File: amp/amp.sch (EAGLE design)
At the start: 73 parts, among them IC1 OPA2134PA, Q1 BC547, Q10 IRF540, Q11 BC556, Q12 BC556, Q13 BC547, Q14 BC547, Q15 2N7000, Q16 BC337, Q17 BC337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

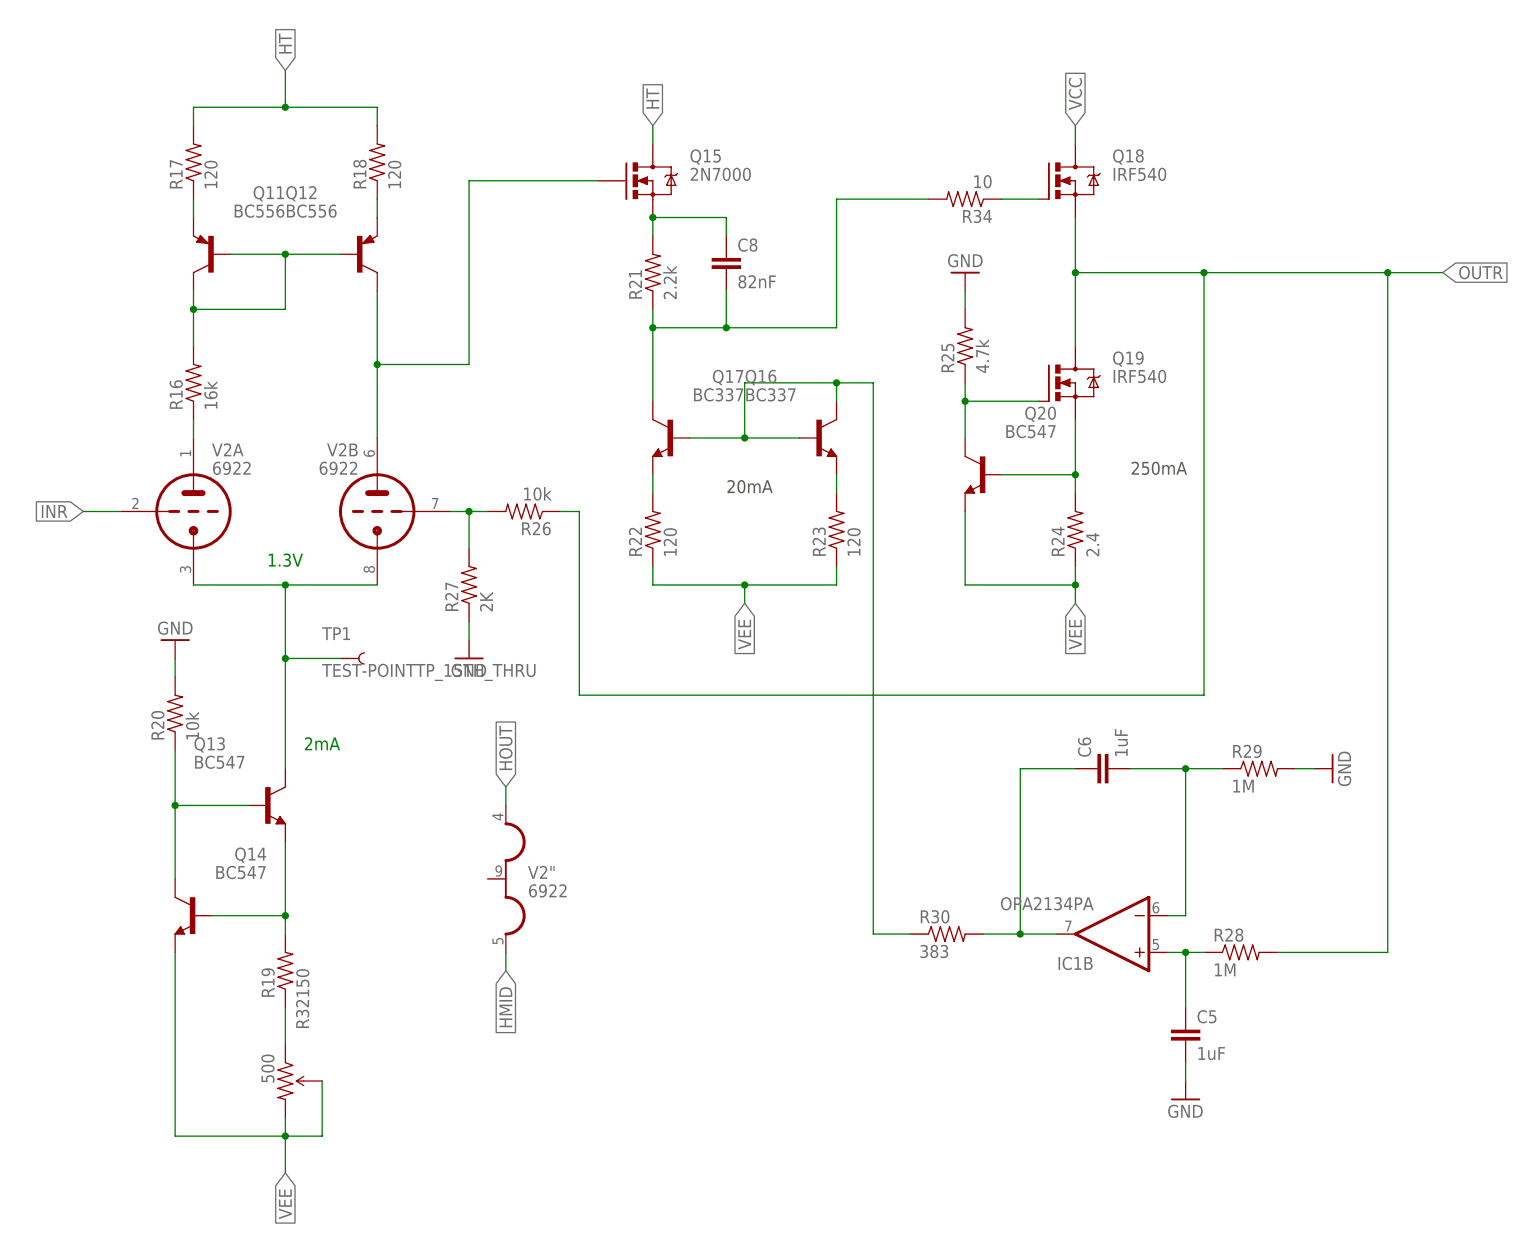
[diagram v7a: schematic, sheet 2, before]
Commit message: High frequency snubber
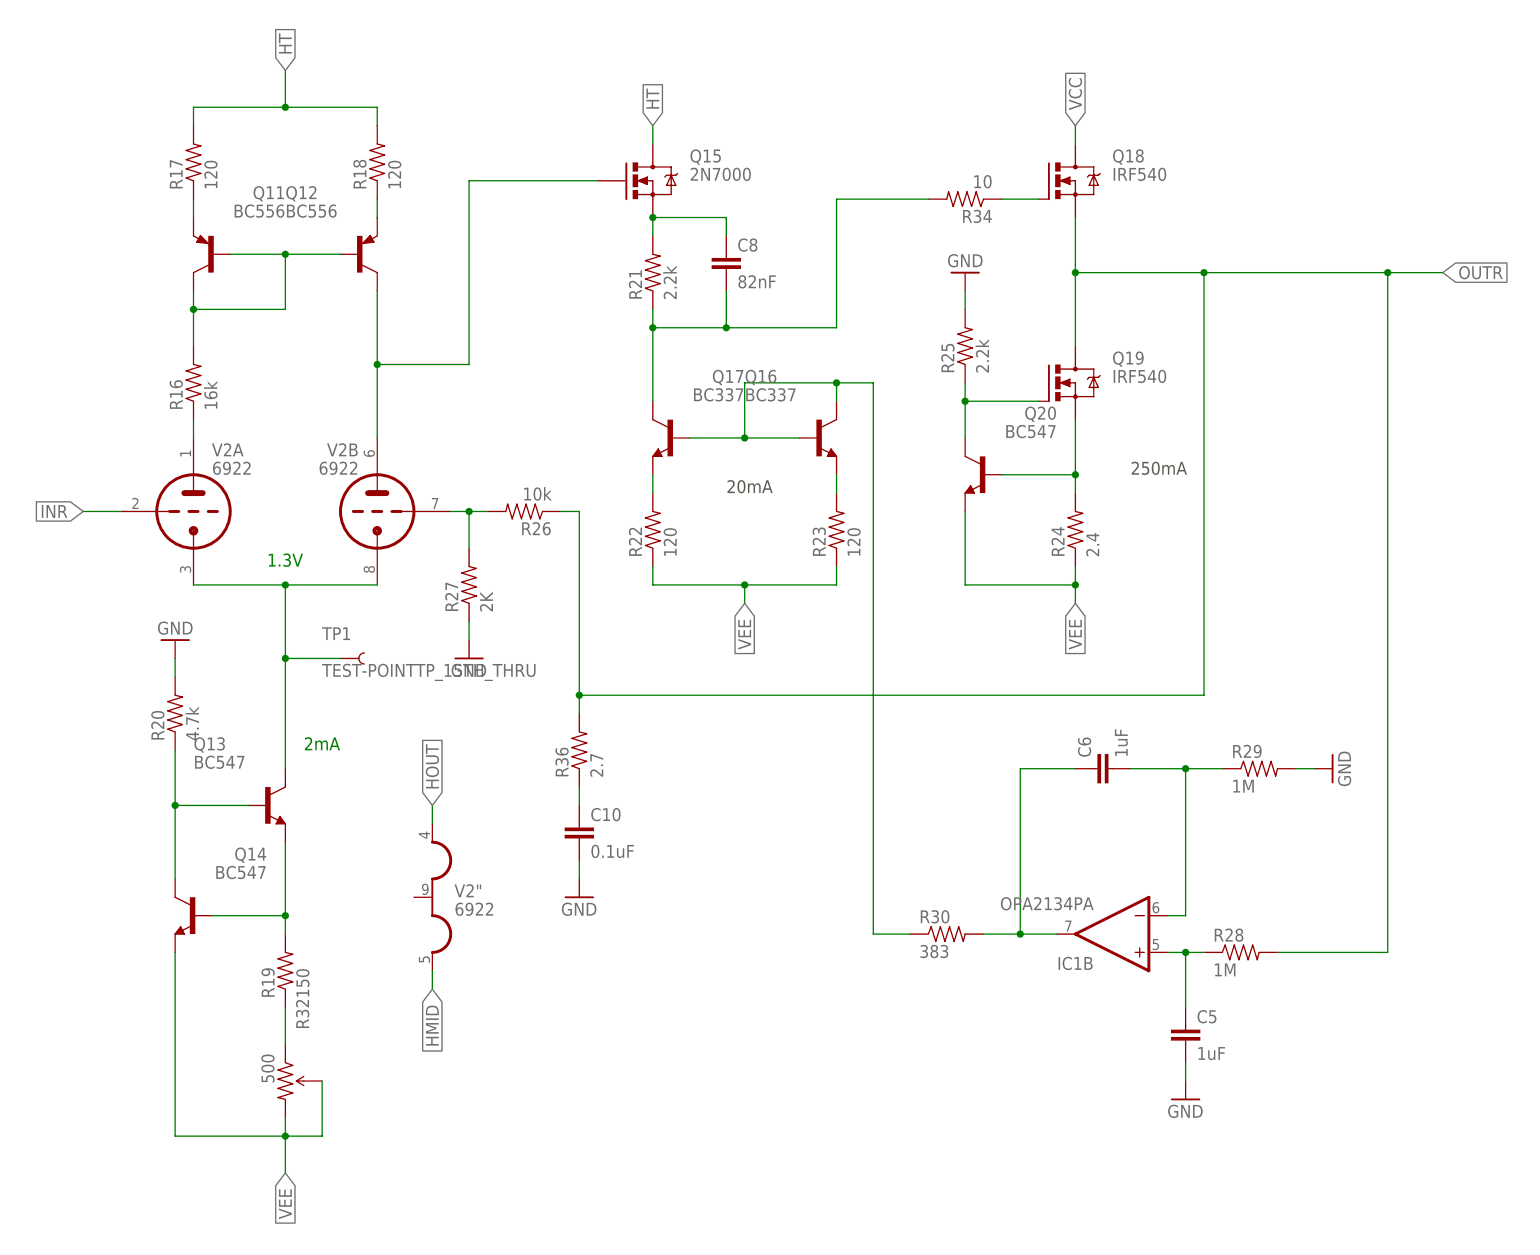
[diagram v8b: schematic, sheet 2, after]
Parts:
- added C10, C9: 0.1uF, SparkFun-Capacitors:0.1UF-25V(+80/-20%)(0603)
- added R35, R36: 2.7, SparkFun-Resistors:RESISTORPTH-1/4W
- R1, R20: value 10k -> 4.7k
- R12: value 10k -> 2.2k
- R25: value 4.7k -> 2.2k
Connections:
- new net N$43: C9.1, R35.1
- new net N$44: C10.1, R36.1
- net GND: now also C10.2, C9.2
- net OUTL: now also R35.2
- net OUTR: now also R36.2
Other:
- moved on the sheet: V2"
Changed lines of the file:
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@@
 <part name="Q1" library="transistor-npn" deviceset="BC547*" device=""/>
 <part name="R4" library="SparkFun-Resistors" deviceset="RESISTOR" device="PTH-1/4W" value="150"/>
-<part name="R1" library="SparkFun-Resistors" deviceset="RESISTOR" device="PTH-1/4W" value="10k"/>
+<part name="R1" library="SparkFun-Resistors" deviceset="RESISTOR" device="PTH-1/4W" value="4.7k"/>
 <part name="GND1" library="SparkFun-Aesthetics" deviceset="GND" device=""/>
 <part name="Q5" library="SparkFun-DiscreteSemi" deviceset="MOSFET-NCHANNEL" device="2N7000" value="2N7000"/>
@@
 <part name="Q8" library="transistor-npn" deviceset="BC547*" device=""/>
 <part name="R13" library="SparkFun-Resistors" deviceset="RESISTOR" device="PTH-1/2W" value="2.4"/>
-<part name="R12" library="SparkFun-Resistors" deviceset="RESISTOR" device="PTH-1/4W" value="10k"/>
+<part name="R12" library="SparkFun-Resistors" deviceset="RESISTOR" device="PTH-1/4W" value="2.2k"/>
 <part name="GND4" library="SparkFun-Aesthetics" deviceset="GND" device=""/>
 <part name="R7" library="SparkFun-Resistors" deviceset="RESISTOR" device="PTH-1/4W" value="10k"/>
@@
 <part name="Q14" library="transistor-npn" deviceset="BC547*" device=""/>
 <part name="R19" library="SparkFun-Resistors" deviceset="RESISTOR" device="PTH-1/4W" value="150"/>
-<part name="R20" library="SparkFun-Resistors" deviceset="RESISTOR" device="PTH-1/4W" value="10k"/>
+<part name="R20" library="SparkFun-Resistors" deviceset="RESISTOR" device="PTH-1/4W" value="4.7k"/>
 <part name="GND8" library="SparkFun-Aesthetics" deviceset="GND" device=""/>
 <part name="Q15" library="SparkFun-DiscreteSemi" deviceset="MOSFET-NCHANNEL" device="2N7000" value="2N7000"/>
@@
 <part name="Q20" library="transistor-npn" deviceset="BC547*" device=""/>
 <part name="R24" library="SparkFun-Resistors" deviceset="RESISTOR" device="PTH-1/2W" value="2.4"/>
-<part name="R25" library="SparkFun-Resistors" deviceset="RESISTOR" device="PTH-1/4W" value="4.7k"/>
+<part name="R25" library="SparkFun-Resistors" deviceset="RESISTOR" device="PTH-1/4W" value="2.2k"/>
 <part name="GND9" library="SparkFun-Aesthetics" deviceset="GND" device=""/>
 <part name="R26" library="SparkFun-Resistors" deviceset="RESISTOR" device="PTH-1/4W" value="10k"/>
@@
 <part name="C7" library="SparkFun-Capacitors" deviceset="1.0UF-25V-+80/-20(0805)" device="&quot;" value="82nF"/>
 <part name="C8" library="SparkFun-Capacitors" deviceset="1.0UF-25V-+80/-20(0805)" device="&quot;" value="82nF"/>
+<part name="C9" library="SparkFun-Capacitors" deviceset="0.1UF-25V(+80/-20%)(0603)" device="" value="0.1uF"/>
+<part name="R35" library="SparkFun-Resistors" deviceset="RESISTOR" device="PTH-1/4W" value="2.7"/>
+<part name="GND13" library="SparkFun-Aesthetics" deviceset="GND" device=""/>
+<part name="C10" library="SparkFun-Capacitors" deviceset="0.1UF-25V(+80/-20%)(0603)" device="" value="0.1uF"/>
+<part name="R36" library="SparkFun-Resistors" deviceset="RESISTOR" device="PTH-1/4W" value="2.7"/>
+<part name="GND14" library="SparkFun-Aesthetics" deviceset="GND" device=""/>
 </parts>
 <sheets>
@@
 <instance part="R33" gate="G$1" x="139.7" y="152.4" rot="R180"/>
 <instance part="C7" gate="G$1" x="106.68" y="142.24"/>
+<instance part="C9" gate="G$1" x="86.36" y="63.5"/>
+<instance part="R35" gate="G$1" x="86.36" y="76.2" rot="R90"/>
+<instance part="GND13" gate="1" x="86.36" y="55.88"/>
 </instances>
 <busses>
@@
 <wire x1="243.84" y1="88.9" x2="246.38" y2="88.9" width="0.1524" layer="91"/>
 <label x="246.38" y="88.9" size="1.778" layer="95" xref="yes"/>
+</segment>
+<segment>
+<pinref part="GND13" gate="1" pin="GND"/>
+<pinref part="C9" gate="G$1" pin="2"/>
+<wire x1="86.36" y1="58.42" x2="86.36" y2="60.96" width="0.1524" layer="91"/>
 </segment>
 </net>
@@
 <wire x1="198.12" y1="48.26" x2="198.12" y2="142.24" width="0.1524" layer="91"/>
 <junction x="198.12" y="142.24"/>
+<pinref part="R35" gate="G$1" pin="2"/>
+<wire x1="86.36" y1="81.28" x2="86.36" y2="83.82" width="0.1524" layer="91"/>
+<junction x="86.36" y="83.82"/>
 </segment>
 <segment>
@@
 <pinref part="R33" gate="G$1" pin="1"/>
 <wire x1="144.78" y1="152.4" x2="149.86" y2="152.4" width="0.1524" layer="91"/>
+</segment>
+</net>
+<net name="N$43" class="0">
+<segment>
+<pinref part="C9" gate="G$1" pin="1"/>
+<pinref part="R35" gate="G$1" pin="1"/>
+<wire x1="86.36" y1="68.58" x2="86.36" y2="71.12" width="0.1524" layer="91"/>
 </segment>
 </net>
@@
 <instance part="GND12" gate="1" x="198.12" y="33.02"/>
 <instance part="R30" gate="G$1" x="165.1" y="55.88"/>
-<instance part="V2" gate="&quot;" x="104.14" y="63.5"/>
+<instance part="V2" gate="&quot;" x="93.98" y="60.96"/>
 <instance part="R32" gate="R?" x="73.66" y="35.56" rot="R270"/>
 <instance part="TP1" gate="G$1" x="81.28" y="93.98"/>
 <instance part="R34" gate="G$1" x="167.64" y="157.48" rot="R180"/>
 <instance part="C8" gate="G$1" x="134.62" y="147.32"/>
+<instance part="C10" gate="G$1" x="114.3" y="68.58"/>
+<instance part="R36" gate="G$1" x="114.3" y="81.28" rot="R90"/>
+<instance part="GND14" gate="1" x="114.3" y="60.96"/>
 </instances>
 <busses>
@@
 <wire x1="198.12" y1="38.1" x2="198.12" y2="35.56" width="0.1524" layer="91"/>
 <pinref part="GND12" gate="1" pin="GND"/>
+</segment>
+<segment>
+<pinref part="GND14" gate="1" pin="GND"/>
+<pinref part="C10" gate="G$1" pin="2"/>
+<wire x1="114.3" y1="63.5" x2="114.3" y2="66.04" width="0.1524" layer="91"/>
 </segment>
 </net>
@@
 <wire x1="226.06" y1="53.34" x2="226.06" y2="147.32" width="0.1524" layer="91"/>
 <junction x="226.06" y="147.32"/>
+<pinref part="R36" gate="G$1" pin="2"/>
+<wire x1="114.3" y1="86.36" x2="114.3" y2="88.9" width="0.1524" layer="91"/>
+<junction x="114.3" y="88.9"/>
 </segment>
 </net>
@@
 <segment>
 <pinref part="V2" gate="&quot;" pin="H3"/>
-<wire x1="104.14" y1="53.34" x2="104.14" y2="50.8" width="0.1524" layer="91"/>
-<label x="104.14" y="50.8" size="1.778" layer="95" rot="R270" xref="yes"/>
+<wire x1="93.98" y1="50.8" x2="93.98" y2="48.26" width="0.1524" layer="91"/>
+<label x="93.98" y="48.26" size="1.778" layer="95" rot="R270" xref="yes"/>
 </segment>
 </net>
@@
 <segment>
 <pinref part="V2" gate="&quot;" pin="H1"/>
-<wire x1="104.14" y1="73.66" x2="104.14" y2="76.2" width="0.1524" layer="91"/>
-<label x="104.14" y="76.2" size="1.778" layer="95" rot="R90" xref="yes"/>
+<wire x1="93.98" y1="71.12" x2="93.98" y2="73.66" width="0.1524" layer="91"/>
+<label x="93.98" y="73.66" size="1.778" layer="95" rot="R90" xref="yes"/>
 </segment>
 </net>
@@
 </segment>
 </net>
+<net name="N$44" class="0">
+<segment>
+<pinref part="C10" gate="G$1" pin="1"/>
+<pinref part="R36" gate="G$1" pin="1"/>
+<wire x1="114.3" y1="73.66" x2="114.3" y2="76.2" width="0.1524" layer="91"/>
+</segment>
+</net>
